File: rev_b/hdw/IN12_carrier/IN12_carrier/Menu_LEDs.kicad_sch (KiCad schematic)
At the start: 25 parts, among them U501 TCA9555RGER

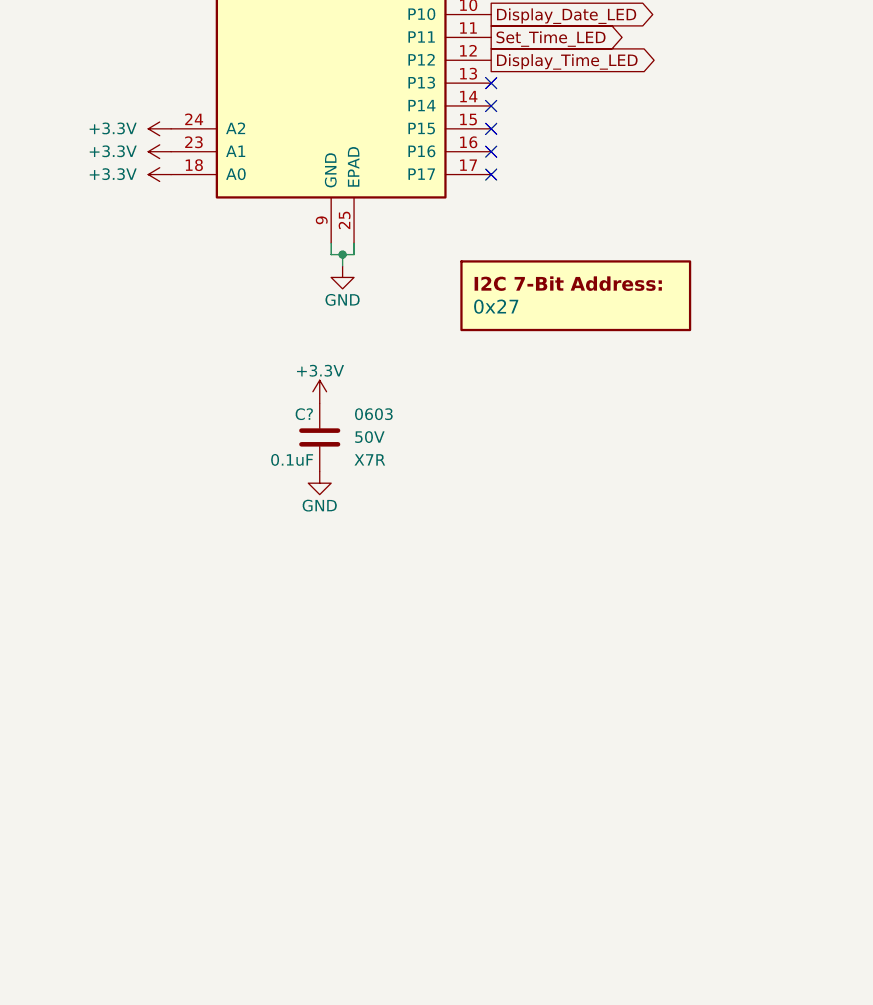
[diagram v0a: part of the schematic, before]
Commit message: updated footprints, ran some DRC
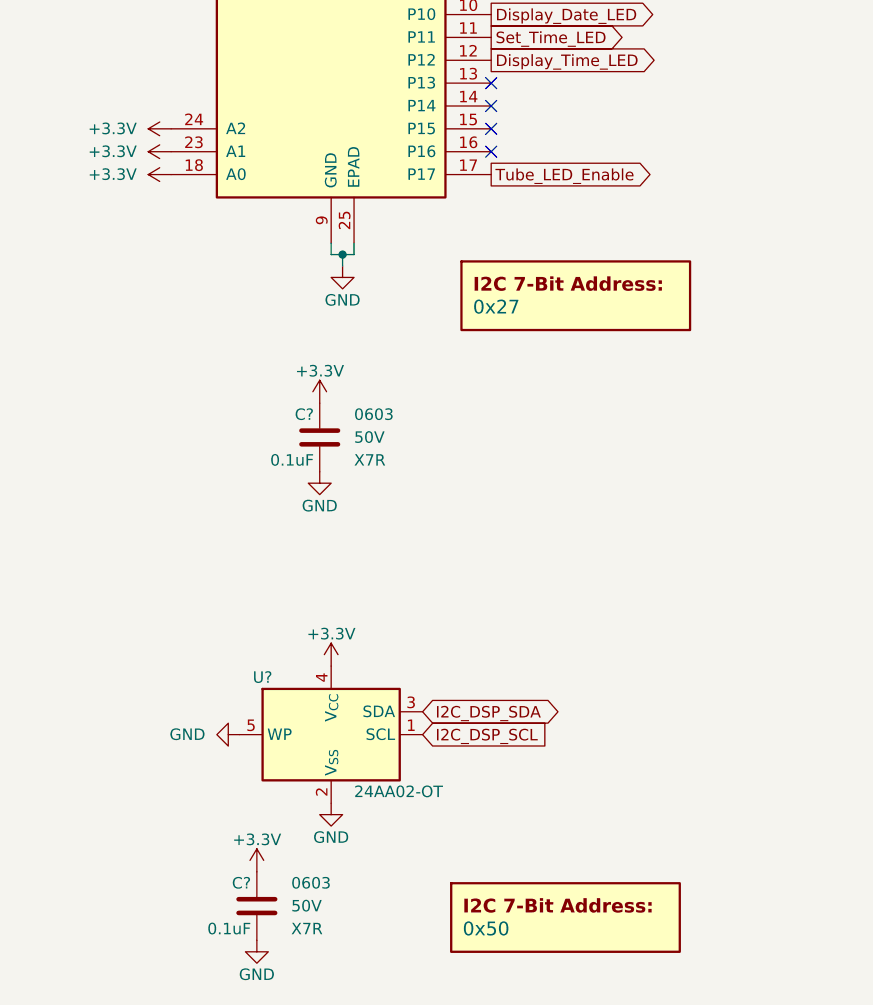
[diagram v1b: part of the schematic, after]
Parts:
- added C?: 0.1uF, Capacitors_SMD:C_0603, symbol Custom_Library:C_Custom
- added DOC501: 0x50, symbol Custom_Library:I2C_Address
- added U?: 24AA02-OT, Package_TO_SOT_SMD:SOT-23-5, symbol Memory_EEPROM:24AA02-OT
- C?: Digi-Key PN 311-1344-1-ND -> (none)
- R? (x11): Digi-Key PN P499HCT-ND -> (none)
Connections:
- net +3.3V: now also C?.1, U?.4 (V_{CC})
- net GND: now also C?.2, U?.2 (V_{SS}), U?.5 (WP)
- net I2C_DSP_SCL: now also U?.1 (SCL)
- net I2C_DSP_SDA: now also U?.3 (SDA)
- net Tube_LED_Enable: now reaches U501.17 (P17)
- no-connect marks 6 -> 5

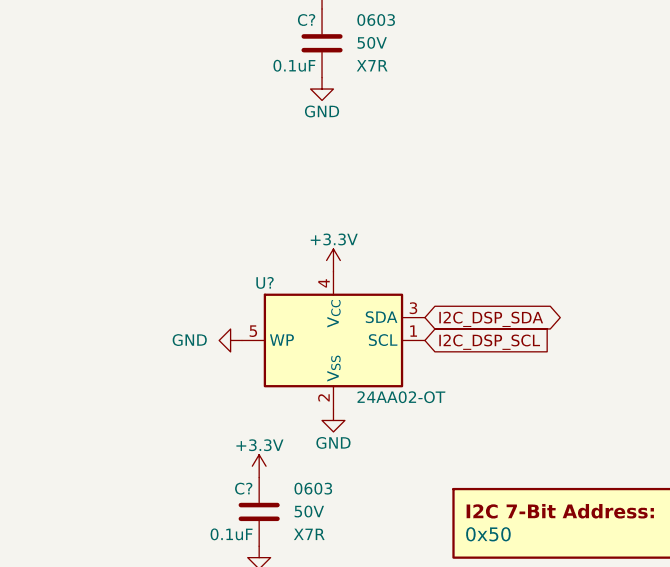
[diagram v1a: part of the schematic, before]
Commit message: annotated, started arranging parts for IN12 carrier
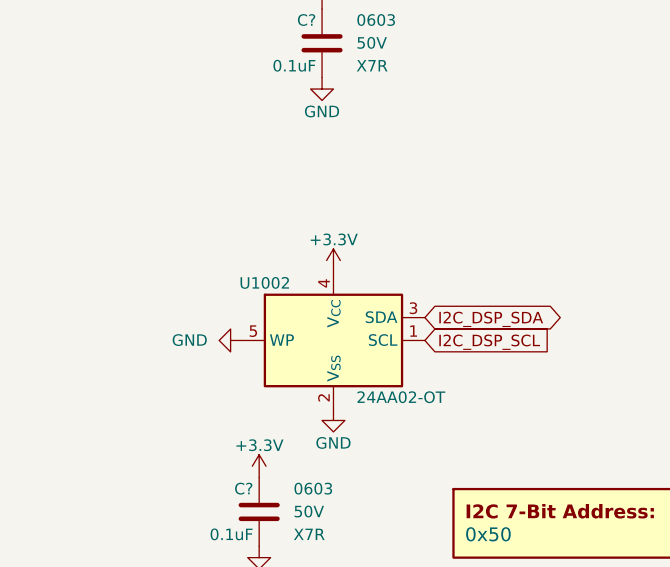
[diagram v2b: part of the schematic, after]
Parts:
- gave numbers to parts that had none: 1
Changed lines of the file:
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@@
       (project "IN12_carrier"
         (path "/c4d83a5b-e6ae-4326-9df5-0c4ac01f7d8c/815dbf76-232e-4bad-8c07-aee05ae43ace"
-          (reference "D?") (unit 1)
+          (reference "D1006") (unit 1)
         )
       )
@@
       (project "IN12_carrier"
         (path "/c4d83a5b-e6ae-4326-9df5-0c4ac01f7d8c/815dbf76-232e-4bad-8c07-aee05ae43ace"
-          (reference "D?") (unit 1)
+          (reference "D1011") (unit 1)
         )
       )
@@
   (symbol (lib_id "Memory_EEPROM:24AA02-OT") (at 80.01 161.29 0) (unit 1)
     (in_bom yes) (on_board yes) (dnp no)
-    (property "Reference" "U?" (at 72.39 154.94 0)
+    (property "Reference" "U1002" (at 72.39 154.94 0)
       (effects (font (size 1.27 1.27)))
     )
@@
       (project "IN12_carrier"
         (path "/c4d83a5b-e6ae-4326-9df5-0c4ac01f7d8c/815dbf76-232e-4bad-8c07-aee05ae43ace"
-          (reference "U?") (unit 1)
+          (reference "U1002") (unit 1)
         )
       )
@@
       (project "IN12_carrier"
         (path "/c4d83a5b-e6ae-4326-9df5-0c4ac01f7d8c/815dbf76-232e-4bad-8c07-aee05ae43ace"
-          (reference "D?") (unit 1)
+          (reference "D1004") (unit 1)
         )
       )
@@
       (project "IN12_carrier"
         (path "/c4d83a5b-e6ae-4326-9df5-0c4ac01f7d8c/815dbf76-232e-4bad-8c07-aee05ae43ace"
-          (reference "R?") (unit 1)
+          (reference "R1004") (unit 1)
         )
       )
@@
       (project "IN12_carrier"
         (path "/c4d83a5b-e6ae-4326-9df5-0c4ac01f7d8c/815dbf76-232e-4bad-8c07-aee05ae43ace"
-          (reference "C?") (unit 1)
+          (reference "C1002") (unit 1)
         )
       )
@@
       (project "IN12_carrier"
         (path "/c4d83a5b-e6ae-4326-9df5-0c4ac01f7d8c/815dbf76-232e-4bad-8c07-aee05ae43ace"
-          (reference "DOC?") (unit 1)
+          (reference "DOC1001") (unit 1)
         )
       )
@@
       (project "IN12_carrier"
         (path "/c4d83a5b-e6ae-4326-9df5-0c4ac01f7d8c/815dbf76-232e-4bad-8c07-aee05ae43ace"
-          (reference "R?") (unit 1)
+          (reference "R1006") (unit 1)
         )
       )
@@
       (project "IN12_carrier"
         (path "/c4d83a5b-e6ae-4326-9df5-0c4ac01f7d8c/815dbf76-232e-4bad-8c07-aee05ae43ace"
-          (reference "D?") (unit 1)
+          (reference "D1010") (unit 1)
         )
       )
@@
       (project "IN12_carrier"
         (path "/c4d83a5b-e6ae-4326-9df5-0c4ac01f7d8c/815dbf76-232e-4bad-8c07-aee05ae43ace"
-          (reference "R?") (unit 1)
+          (reference "R1010") (unit 1)
         )
       )
@@
       (project "IN12_carrier"
         (path "/c4d83a5b-e6ae-4326-9df5-0c4ac01f7d8c/815dbf76-232e-4bad-8c07-aee05ae43ace"
-          (reference "R?") (unit 1)
+          (reference "R1009") (unit 1)
         )
       )
@@
       (project "IN12_carrier"
         (path "/c4d83a5b-e6ae-4326-9df5-0c4ac01f7d8c/815dbf76-232e-4bad-8c07-aee05ae43ace"
-          (reference "R?") (unit 1)
+          (reference "R1007") (unit 1)
         )
       )
@@
       (project "IN12_carrier"
         (path "/c4d83a5b-e6ae-4326-9df5-0c4ac01f7d8c/815dbf76-232e-4bad-8c07-aee05ae43ace"
-          (reference "R?") (unit 1)
+          (reference "R1002") (unit 1)
         )
       )
@@
       (project "IN12_carrier"
         (path "/c4d83a5b-e6ae-4326-9df5-0c4ac01f7d8c/815dbf76-232e-4bad-8c07-aee05ae43ace"
-          (reference "D?") (unit 1)
+          (reference "D1002") (unit 1)
         )
       )
@@
       (project "IN12_carrier"
         (path "/c4d83a5b-e6ae-4326-9df5-0c4ac01f7d8c/815dbf76-232e-4bad-8c07-aee05ae43ace"
-          (reference "D?") (unit 1)
+          (reference "D1005") (unit 1)
         )
       )
@@
       (project "IN12_carrier"
         (path "/c4d83a5b-e6ae-4326-9df5-0c4ac01f7d8c/815dbf76-232e-4bad-8c07-aee05ae43ace"
-          (reference "D?") (unit 1)
+          (reference "D1007") (unit 1)
         )
       )
@@
       (project "IN12_carrier"
         (path "/c4d83a5b-e6ae-4326-9df5-0c4ac01f7d8c/815dbf76-232e-4bad-8c07-aee05ae43ace"
-          (reference "R?") (unit 1)
+          (reference "R1008") (unit 1)
         )
       )
@@
       (project "IN12_carrier"
         (path "/c4d83a5b-e6ae-4326-9df5-0c4ac01f7d8c/815dbf76-232e-4bad-8c07-aee05ae43ace"
-          (reference "R?") (unit 1)
+          (reference "R1003") (unit 1)
         )
       )
@@
       (project "IN12_carrier"
         (path "/c4d83a5b-e6ae-4326-9df5-0c4ac01f7d8c/815dbf76-232e-4bad-8c07-aee05ae43ace"
-          (reference "D?") (unit 1)
+          (reference "D1009") (unit 1)
         )
       )
@@
       (project "IN12_carrier"
         (path "/c4d83a5b-e6ae-4326-9df5-0c4ac01f7d8c/815dbf76-232e-4bad-8c07-aee05ae43ace"
-          (reference "DOC?") (unit 1)
+          (reference "DOC1002") (unit 1)
         )
       )
@@
       (project "IN12_carrier"
         (path "/c4d83a5b-e6ae-4326-9df5-0c4ac01f7d8c/815dbf76-232e-4bad-8c07-aee05ae43ace"
-          (reference "R?") (unit 1)
+          (reference "R1005") (unit 1)
         )
       )
@@
       (project "IN12_carrier"
         (path "/c4d83a5b-e6ae-4326-9df5-0c4ac01f7d8c/815dbf76-232e-4bad-8c07-aee05ae43ace"
-          (reference "D?") (unit 1)
+          (reference "D1003") (unit 1)
         )
       )
@@
       (project "IN12_carrier"
         (path "/c4d83a5b-e6ae-4326-9df5-0c4ac01f7d8c/815dbf76-232e-4bad-8c07-aee05ae43ace"
-          (reference "R?") (unit 1)
+          (reference "R1011") (unit 1)
         )
       )
@@
       (project "IN12_carrier"
         (path "/c4d83a5b-e6ae-4326-9df5-0c4ac01f7d8c/815dbf76-232e-4bad-8c07-aee05ae43ace"
-          (reference "U?") (unit 1)
+          (reference "U1001") (unit 1)
         )
       )
@@
       (project "IN12_carrier"
         (path "/c4d83a5b-e6ae-4326-9df5-0c4ac01f7d8c/815dbf76-232e-4bad-8c07-aee05ae43ace"
-          (reference "D?") (unit 1)
+          (reference "D1008") (unit 1)
         )
       )
@@
       (project "IN12_carrier"
         (path "/c4d83a5b-e6ae-4326-9df5-0c4ac01f7d8c/815dbf76-232e-4bad-8c07-aee05ae43ace"
-          (reference "R?") (unit 1)
+          (reference "R1001") (unit 1)
         )
       )
@@
       (project "IN12_carrier"
         (path "/c4d83a5b-e6ae-4326-9df5-0c4ac01f7d8c/815dbf76-232e-4bad-8c07-aee05ae43ace"
-          (reference "D?") (unit 1)
+          (reference "D1001") (unit 1)
         )
       )
@@
       (project "IN12_carrier"
         (path "/c4d83a5b-e6ae-4326-9df5-0c4ac01f7d8c/815dbf76-232e-4bad-8c07-aee05ae43ace"
-          (reference "C?") (unit 1)
-        )
-      )
+          (reference "C1001") (unit 1)
+        )
+      )

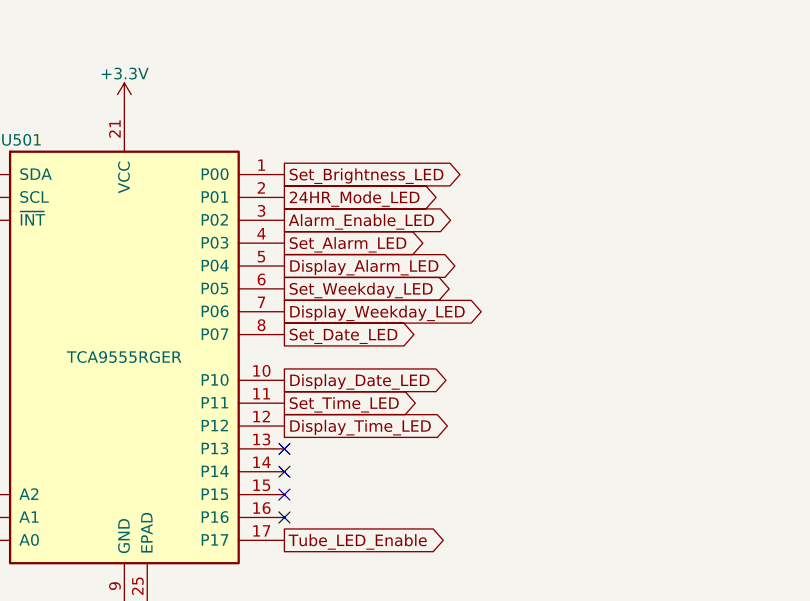
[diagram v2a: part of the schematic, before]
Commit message: all components within IN12 carrier board outline
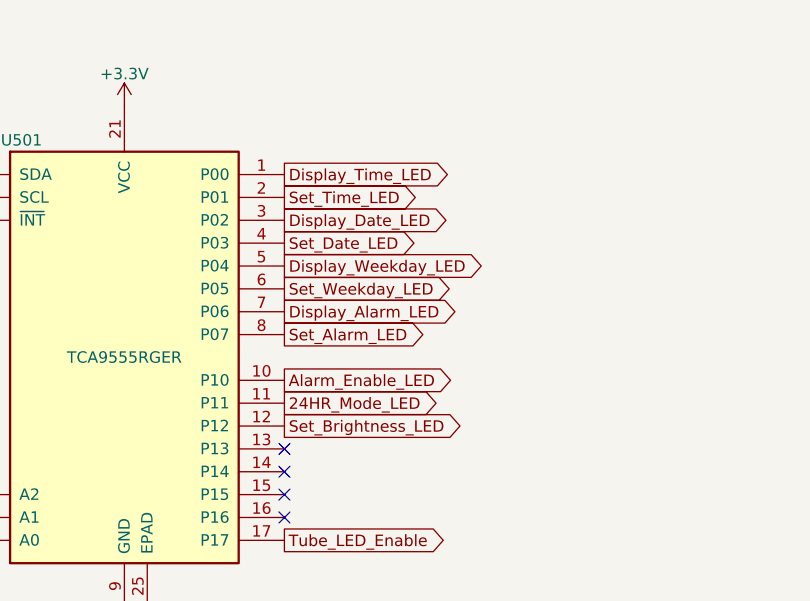
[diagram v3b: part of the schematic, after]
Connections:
- net 24HR_Mode_LED: now also U501.11 (P11); no longer U501.2 (P01)
- net Alarm_Enable_LED: now also U501.10 (P10); no longer U501.3 (P02)
- net Display_Alarm_LED: now also U501.7 (P06); no longer U501.5 (P04)
- net Display_Date_LED: now also U501.3 (P02); no longer U501.10 (P10)
- net Display_Time_LED: now also U501.1 (P00); no longer U501.12 (P12)
- net Display_Weekday_LED: now also U501.5 (P04); no longer U501.7 (P06)
- net Set_Alarm_LED: now also U501.8 (P07); no longer U501.4 (P03)
- net Set_Brightness_LED: now also U501.12 (P12); no longer U501.1 (P00)
- net Set_Date_LED: now also U501.4 (P03); no longer U501.8 (P07)
- net Set_Time_LED: now also U501.2 (P01); no longer U501.11 (P11)
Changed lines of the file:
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@@
     )
   )
-  (global_label "Set_Date_LED" (shape output) (at 97.79 76.2 0)
+  (global_label "Set_Date_LED" (shape output) (at 97.79 66.04 0)
     (effects (font (size 1.27 1.27)) (justify left))
-    (property "Intersheetrefs" "${INTERSHEET_REFS}" (at 97.79 76.2 0)
+    (property "Intersheetrefs" "${INTERSHEET_REFS}" (at 97.79 66.04 0)
       (effects (font (size 1.27 1.27)) hide)
     )
@@
     )
   )
-  (global_label "Display_Weekday_LED" (shape output) (at 97.79 73.66 0)
+  (global_label "Display_Weekday_LED" (shape output) (at 97.79 68.58 0)
     (effects (font (size 1.27 1.27)) (justify left))
-    (property "Intersheetrefs" "${INTERSHEET_REFS}" (at 97.79 73.66 0)
+    (property "Intersheetrefs" "${INTERSHEET_REFS}" (at 97.79 68.58 0)
       (effects (font (size 1.27 1.27)) hide)
     )
@@
     )
   )
-  (global_label "Display_Time_LED" (shape output) (at 97.79 86.36 0)
+  (global_label "Display_Time_LED" (shape output) (at 97.79 58.42 0)
     (effects (font (size 1.27 1.27)) (justify left))
-    (property "Intersheetrefs" "${INTERSHEET_REFS}" (at 97.79 86.36 0)
+    (property "Intersheetrefs" "${INTERSHEET_REFS}" (at 97.79 58.42 0)
       (effects (font (size 1.27 1.27)) hide)
     )
@@
     )
   )
-  (global_label "Display_Alarm_LED" (shape output) (at 97.79 68.58 0)
+  (global_label "Display_Alarm_LED" (shape output) (at 97.79 73.66 0)
     (effects (font (size 1.27 1.27)) (justify left))
-    (property "Intersheetrefs" "${INTERSHEET_REFS}" (at 97.79 68.58 0)
+    (property "Intersheetrefs" "${INTERSHEET_REFS}" (at 97.79 73.66 0)
       (effects (font (size 1.27 1.27)) hide)
     )
   )
-  (global_label "Set_Time_LED" (shape output) (at 97.79 83.82 0)
+  (global_label "Set_Time_LED" (shape output) (at 97.79 60.96 0)
     (effects (font (size 1.27 1.27)) (justify left))
-    (property "Intersheetrefs" "${INTERSHEET_REFS}" (at 97.79 83.82 0)
+    (property "Intersheetrefs" "${INTERSHEET_REFS}" (at 97.79 60.96 0)
       (effects (font (size 1.27 1.27)) hide)
     )
@@
     )
   )
-  (global_label "24HR_Mode_LED" (shape output) (at 97.79 60.96 0)
+  (global_label "24HR_Mode_LED" (shape output) (at 97.79 83.82 0)
     (effects (font (size 1.27 1.27)) (justify left))
-    (property "Intersheetrefs" "${INTERSHEET_REFS}" (at 97.79 60.96 0)
+    (property "Intersheetrefs" "${INTERSHEET_REFS}" (at 97.79 83.82 0)
       (effects (font (size 1.27 1.27)) hide)
     )
@@
     )
   )
-  (global_label "Display_Date_LED" (shape output) (at 97.79 81.28 0)
+  (global_label "Display_Date_LED" (shape output) (at 97.79 63.5 0)
     (effects (font (size 1.27 1.27)) (justify left))
-    (property "Intersheetrefs" "${INTERSHEET_REFS}" (at 97.79 81.28 0)
+    (property "Intersheetrefs" "${INTERSHEET_REFS}" (at 97.79 63.5 0)
       (effects (font (size 1.27 1.27)) hide)
     )
   )
-  (global_label "Set_Brightness_LED" (shape output) (at 97.79 58.42 0)
+  (global_label "Set_Brightness_LED" (shape output) (at 97.79 86.36 0)
     (effects (font (size 1.27 1.27)) (justify left))
-    (property "Intersheetrefs" "${INTERSHEET_REFS}" (at 97.79 58.42 0)
+    (property "Intersheetrefs" "${INTERSHEET_REFS}" (at 97.79 86.36 0)
       (effects (font (size 1.27 1.27)) hide)
     )
   )
-  (global_label "Set_Alarm_LED" (shape output) (at 97.79 66.04 0)
+  (global_label "Set_Alarm_LED" (shape output) (at 97.79 76.2 0)
     (effects (font (size 1.27 1.27)) (justify left))
-    (property "Intersheetrefs" "${INTERSHEET_REFS}" (at 97.79 66.04 0)
+    (property "Intersheetrefs" "${INTERSHEET_REFS}" (at 97.79 76.2 0)
       (effects (font (size 1.27 1.27)) hide)
     )
@@
     )
   )
-  (global_label "Alarm_Enable_LED" (shape output) (at 97.79 63.5 0)
+  (global_label "Alarm_Enable_LED" (shape output) (at 97.79 81.28 0)
     (effects (font (size 1.27 1.27)) (justify left))
-    (property "Intersheetrefs" "${INTERSHEET_REFS}" (at 97.79 63.5 0)
+    (property "Intersheetrefs" "${INTERSHEET_REFS}" (at 97.79 81.28 0)
       (effects (font (size 1.27 1.27)) hide)
     )
